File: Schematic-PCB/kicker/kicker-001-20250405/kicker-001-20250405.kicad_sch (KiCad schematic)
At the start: 24 parts, among them J1 VIN, J2 VOUT, J3 toWhere?, Q1 NMOS, Q2 Photo, U2 TLP2361, U3 74AHC1G04

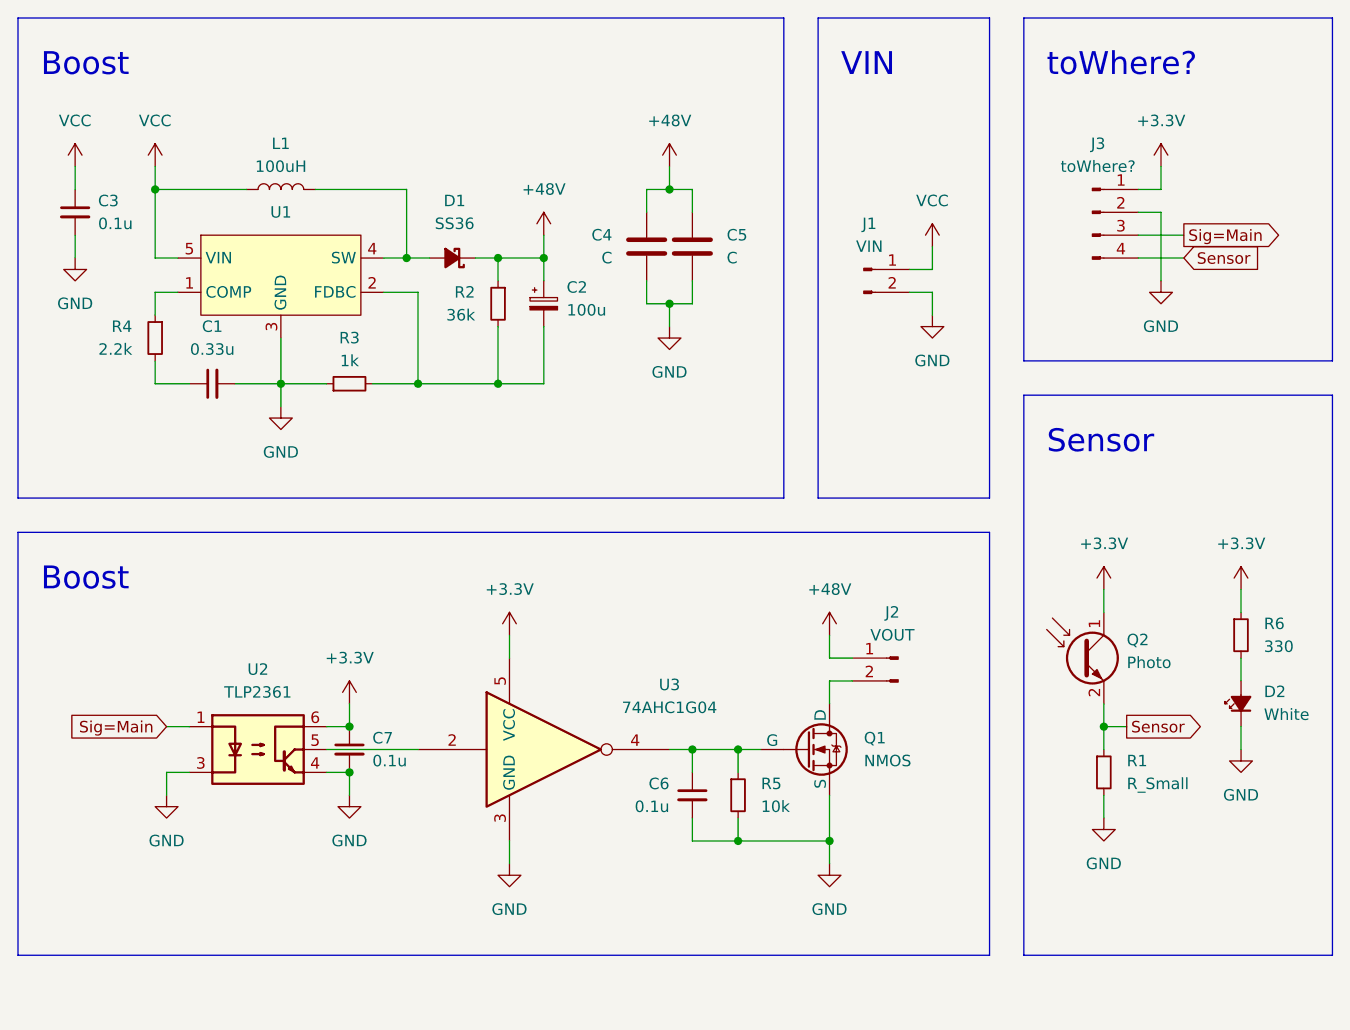
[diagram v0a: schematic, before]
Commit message: update: キッカー基板の回路図をchatGPTのDRをもとに修正
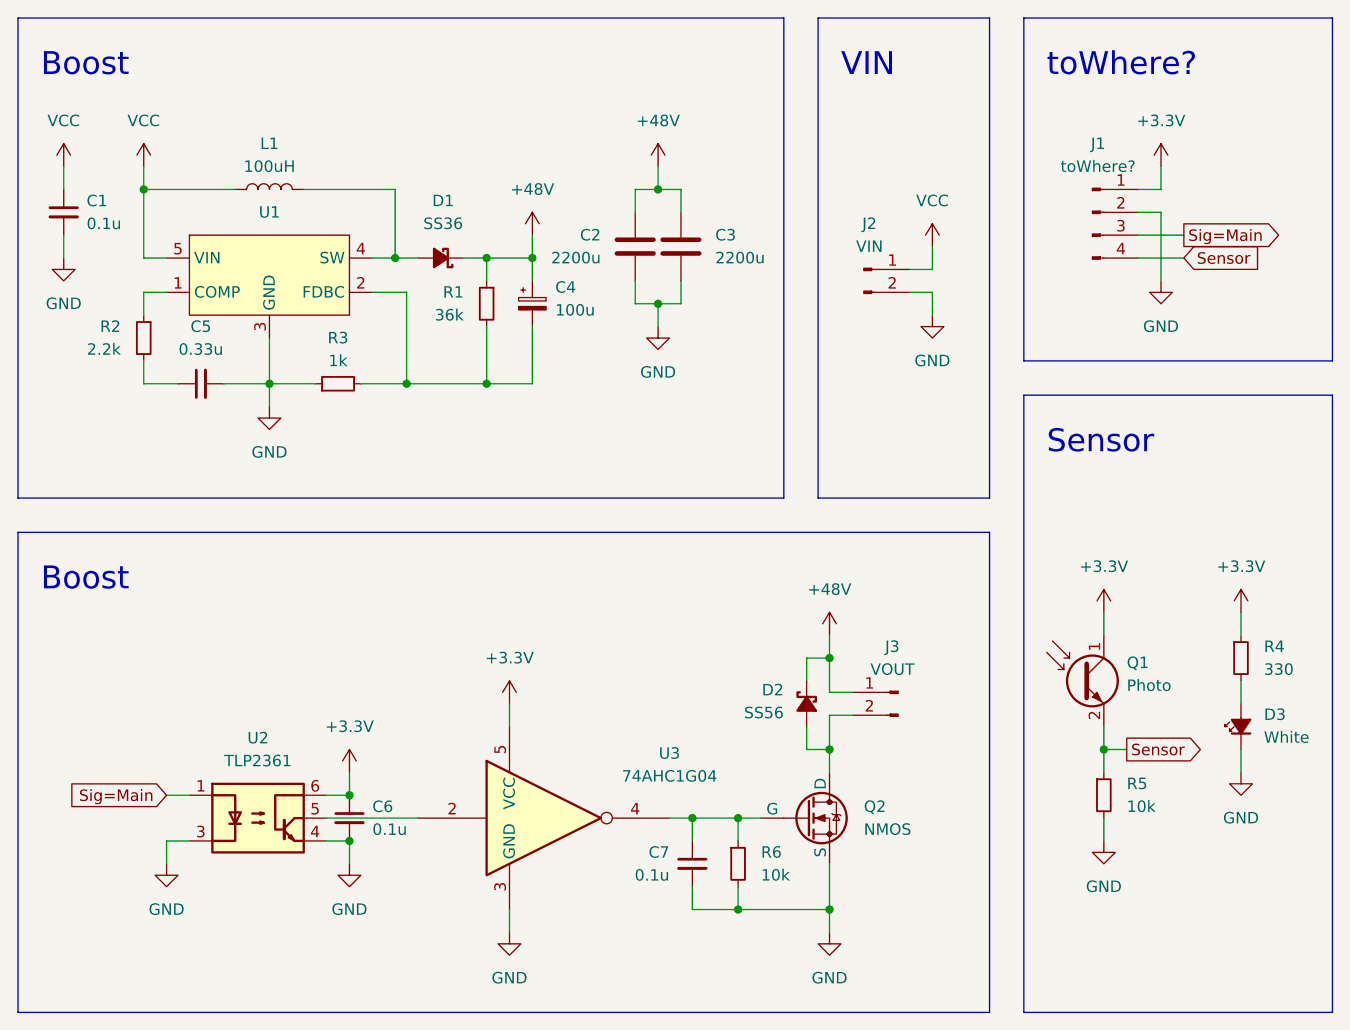
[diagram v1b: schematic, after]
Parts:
- added D2: SS56, Diode_SMD:D_SMB, symbol Device:D_Schottky_Small_Filled
- C1: renamed from C3; footprint (none) -> Capacitor_SMD:C_0603_1608Metric
- C2: renamed from C4; value C -> 2200u; footprint (none) -> Capacitor_THT:CP_Radial_D13.0mm_P7.50mm
- C3: renamed from C5; value C -> 2200u; footprint (none) -> Capacitor_THT:CP_Radial_D13.0mm_P7.50mm
- C4: renamed from C2; footprint (none) -> Capacitor_SMD:C_0603_1608Metric
- C5: renamed from C1; footprint (none) -> Capacitor_SMD:C_0603_1608Metric
- C6: renamed from C7; footprint (none) -> Capacitor_SMD:C_0603_1608Metric
- C7: renamed from C6; footprint (none) -> Capacitor_SMD:C_0603_1608Metric
- D1: footprint (none) -> Diode_SMD:D_SMA
- D3: renamed from D2; footprint (none) -> LED_THT:LED_D3.0mm
- J2: renamed from J1; footprint (none) -> Connector_JST:JST_XH_B2B-XH-A_1x02_P2.50mm_Vertical
- J3: renamed from J2; footprint (none) -> Connector_JST:JST_XH_B2B-XH-A_1x02_P2.50mm_Vertical
- L1: footprint (none) -> Inductor_SMD:L_12x12mm_H8mm
- R1: renamed from R2; footprint (none) -> Resistor_SMD:R_0603_1608Metric
- R2: renamed from R4; footprint (none) -> Resistor_SMD:R_0603_1608Metric
- R3: footprint (none) -> Resistor_SMD:R_0603_1608Metric
- R4: renamed from R6; footprint (none) -> Resistor_SMD:R_0603_1608Metric
- R5: renamed from R1; value R_Small -> 10k; footprint (none) -> Resistor_SMD:R_0603_1608Metric
- R6: renamed from R5; footprint (none) -> Resistor_SMD:R_0603_1608Metric
- renumbered J3 to J1, Q2 to Q1, Q1 to Q2
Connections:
- net +48V: now also D2.1 (K)
- net at J3.2 (Pin_2), Q2.1 (D): now also D2.2 (A)
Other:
- moved on the sheet: C1, C2, C3, C4, C5, C6, C7, D1, D3, J3, L1, Q1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
